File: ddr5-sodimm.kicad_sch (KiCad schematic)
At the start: 1 part, among them J4001 BUS_DDR5_SODIMM_AMPHENOL_1016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

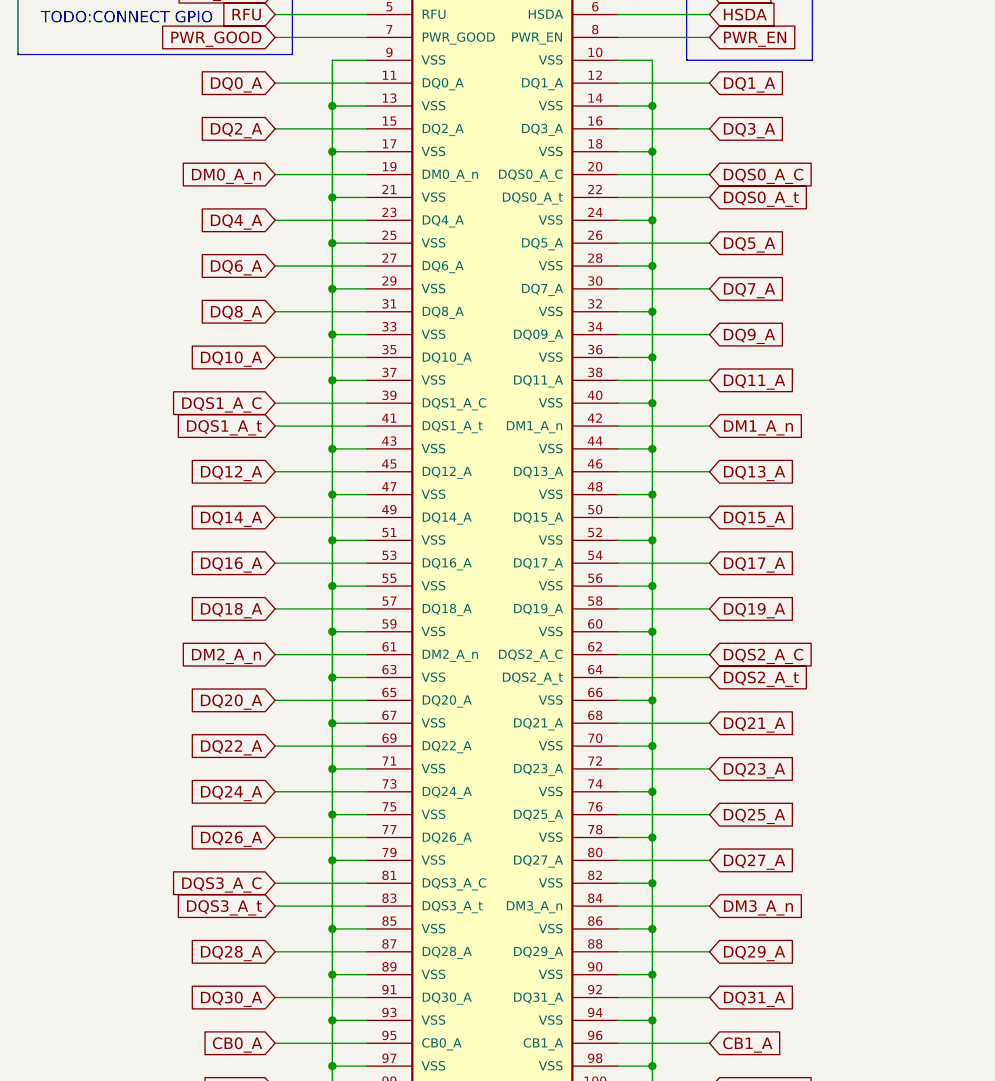
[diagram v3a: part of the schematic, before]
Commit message: Create pinout and fanout for FPGA bank 32
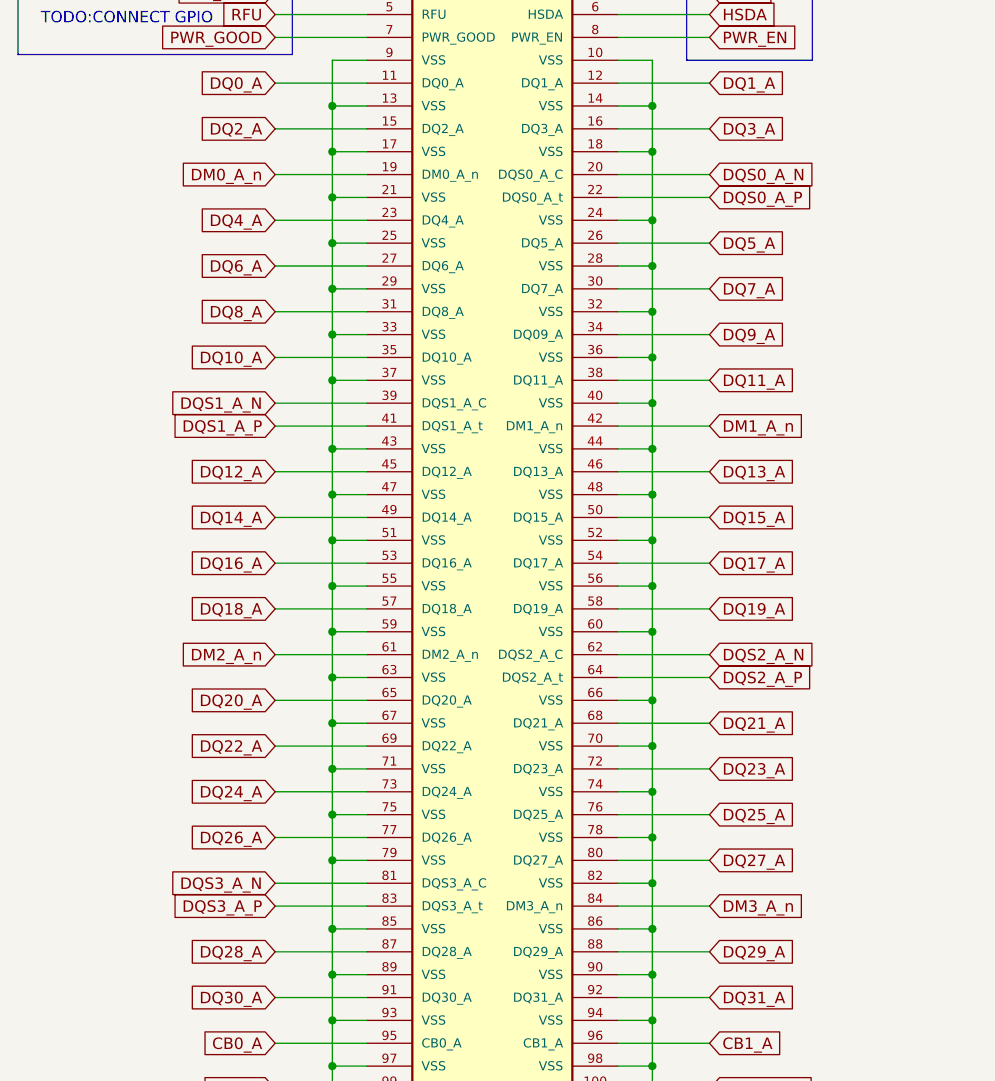
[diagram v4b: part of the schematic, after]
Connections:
- net DQS0_A_C renamed DQS0_A_N
- net DQS0_A_t renamed DQS0_A_P
- net DQS1_A_C renamed DQS1_A_N
- net DQS1_A_t renamed DQS1_A_P
- net DQS2_A_C renamed DQS2_A_N
- net DQS2_A_t renamed DQS2_A_P
- net DQS3_A_C renamed DQS3_A_N
- net DQS3_A_t renamed DQS3_A_P
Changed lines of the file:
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@@
     )
   )
-  (global_label "DQS2_A_t" (shape input) (at 137.795 130.175 0) (fields_autoplaced)
-    (effects (font (size 1.27 1.27)) (justify left))
-    (property "Intersheet References" "${INTERSHEET_REFS}" (id 0) (at 148.8882 130.0956 0)
+  (global_label "DQS2_A_P" (shape input) (at 137.795 130.175 0) (fields_autoplaced)
+    (effects (font (size 1.27 1.27)) (justify left))
+    (property "Intersheet References" "${INTERSHEET_REFS}" (id 0) (at 149.4325 130.0956 0)
       (effects (font (size 1.27 1.27)) (justify left) hide)
     )
@@
     )
   )
-  (global_label "DQS1_A_C" (shape input) (at 89.535 99.695 180) (fields_autoplaced)
-    (effects (font (size 1.27 1.27)) (justify right))
-    (property "Intersheet References" "${INTERSHEET_REFS}" (id 0) (at 77.8975 99.7744 0)
+  (global_label "DQS1_A_N" (shape input) (at 89.535 99.695 180) (fields_autoplaced)
+    (effects (font (size 1.27 1.27)) (justify right))
+    (property "Intersheet References" "${INTERSHEET_REFS}" (id 0) (at 77.837 99.6156 0)
       (effects (font (size 1.27 1.27)) (justify right) hide)
     )
@@
     )
   )
-  (global_label "DQS1_A_t" (shape input) (at 89.535 102.235 180) (fields_autoplaced)
-    (effects (font (size 1.27 1.27)) (justify right))
-    (property "Intersheet References" "${INTERSHEET_REFS}" (id 0) (at 78.4418 102.1556 0)
+  (global_label "DQS1_A_P" (shape input) (at 89.535 102.235 180) (fields_autoplaced)
+    (effects (font (size 1.27 1.27)) (justify right))
+    (property "Intersheet References" "${INTERSHEET_REFS}" (id 0) (at 77.8975 102.1556 0)
       (effects (font (size 1.27 1.27)) (justify right) hide)
     )
@@
     )
   )
-  (global_label "DQS3_A_t" (shape input) (at 89.535 155.575 180) (fields_autoplaced)
-    (effects (font (size 1.27 1.27)) (justify right))
-    (property "Intersheet References" "${INTERSHEET_REFS}" (id 0) (at 78.4418 155.4956 0)
+  (global_label "DQS3_A_P" (shape input) (at 89.535 155.575 180) (fields_autoplaced)
+    (effects (font (size 1.27 1.27)) (justify right))
+    (property "Intersheet References" "${INTERSHEET_REFS}" (id 0) (at 77.8975 155.4956 0)
       (effects (font (size 1.27 1.27)) (justify right) hide)
     )
@@
     )
   )
-  (global_label "DQS0_A_C" (shape input) (at 137.795 74.295 0) (fields_autoplaced)
-    (effects (font (size 1.27 1.27)) (justify left))
-    (property "Intersheet References" "${INTERSHEET_REFS}" (id 0) (at 149.4325 74.2156 0)
+  (global_label "DQS0_A_N" (shape input) (at 137.795 74.295 0) (fields_autoplaced)
+    (effects (font (size 1.27 1.27)) (justify left))
+    (property "Intersheet References" "${INTERSHEET_REFS}" (id 0) (at 149.493 74.2156 0)
       (effects (font (size 1.27 1.27)) (justify left) hide)
     )
@@
     )
   )
-  (global_label "DQS0_A_t" (shape input) (at 137.795 76.835 0) (fields_autoplaced)
-    (effects (font (size 1.27 1.27)) (justify left))
-    (property "Intersheet References" "${INTERSHEET_REFS}" (id 0) (at 148.8882 76.7556 0)
+  (global_label "DQS0_A_P" (shape input) (at 137.795 76.835 0) (fields_autoplaced)
+    (effects (font (size 1.27 1.27)) (justify left))
+    (property "Intersheet References" "${INTERSHEET_REFS}" (id 0) (at 149.4325 76.7556 0)
       (effects (font (size 1.27 1.27)) (justify left) hide)
     )
@@
     )
   )
-  (global_label "DQS3_A_C" (shape input) (at 89.535 153.035 180) (fields_autoplaced)
-    (effects (font (size 1.27 1.27)) (justify right))
-    (property "Intersheet References" "${INTERSHEET_REFS}" (id 0) (at 77.8975 152.9556 0)
+  (global_label "DQS3_A_N" (shape input) (at 89.535 153.035 180) (fields_autoplaced)
+    (effects (font (size 1.27 1.27)) (justify right))
+    (property "Intersheet References" "${INTERSHEET_REFS}" (id 0) (at 77.837 152.9556 0)
       (effects (font (size 1.27 1.27)) (justify right) hide)
     )
@@
     )
   )
-  (global_label "DQS2_A_C" (shape input) (at 137.795 127.635 0) (fields_autoplaced)
-    (effects (font (size 1.27 1.27)) (justify left))
-    (property "Intersheet References" "${INTERSHEET_REFS}" (id 0) (at 149.4325 127.5556 0)
-      (effects (font (size 1.27 1.27)) (justify left) hide)
-    )
+  (global_label "DQS2_A_N" (shape input) (at 137.795 127.635 0) (fields_autoplaced)
+    (effects (font (size 1.27 1.27)) (justify left))
+    (property "Intersheet References" "${INTERSHEET_REFS}" (id 0) (at 149.493 127.5556 0)
+      (effects (font (size 1.27 1.27)) (justify left) hide)
+    )
